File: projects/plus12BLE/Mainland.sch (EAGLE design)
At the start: 69 parts, among them J1 USB-CWM2.0, SW1 RSTSWSMD, SW2 RSTSWSMD, U1 BL652-SA-01-T/R, U2 MCP73831T-2ACI/OT, U4 CP2102N-A01-GQFN20

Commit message: working for DFM, new USB connector test
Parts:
- removed JP2: (no value), pinhead:PINHD-1X4
- removed JP3: (no value), pinhead:PINHD-1X5/90
- added J2: RA 6Pin SMD, SparkFun-Connectors:CONN_04SMD_RA_FEMALE
- added J3: RA 6Pin SMD, SparkFun-Connectors:CONN_06SMD
- C4, C6: device resistor:C-USC0402K -> resistor:C-USC0603
- R1, R10, R2, R3, R4, R5, R6, R7, R8, R9: device resistor:R-US_R0402 -> resistor:R-US_R0603
- SW1, SW2: value RSTSWSMD -> RSTSWSMALL_SMD; device Keys:RSTSWSMD -> Keys:RSTSWSMALL_SMD
- renumbered U$3 to SW3
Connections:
- net 3.3V: now also J2.4; no longer JP2.1, JP3.1
- net GND: now also J2.1, J3.1; no longer JP2.4, JP3.5
- net RX0: now also J3.5; no longer JP3.2
- net SWDCLK: now also J2.2; no longer JP2.3
- net SWDIO: now also J2.3; no longer JP2.2
- net TX0: now also J3.4; no longer JP3.3
- net V_USB: now also J3.3; no longer JP3.4
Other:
- note added: "Can also charge through V_USB and GND on this header"
- note added: "UART (RX/TX) Used in place of CP2104 QFN. MUST USE 3.3V LOGIC"
- note removed: "Also breaking out +5V Vbus/V_USB if soldering USBC is a difficulty"
- note removed: "UART (RX/TX) Used in place of CP2104 QFN"

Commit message: saving before autorouter
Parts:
- J1: value USB-CWM2.0 -> USB-C2.0WM2.0; device Keys:USB-CWM2.0 -> Keys:USB-C2.0WM2.0
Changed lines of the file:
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@@
 <grid distance="0.1" unitdist="inch" unit="inch" style="lines" multiple="1" display="no" altdistance="0.01" altunitdist="inch" altunit="inch"/>
 <layers>
-<layer number="1" name="Top" color="4" fill="1" visible="yes" active="no"/>
-<layer number="2" name="Route2" color="16" fill="1" visible="yes" active="no"/>
-<layer number="3" name="Route3" color="17" fill="1" visible="yes" active="no"/>
-<layer number="4" name="Route4" color="18" fill="1" visible="yes" active="no"/>
-<layer number="5" name="Route5" color="19" fill="1" visible="yes" active="no"/>
-<layer number="6" name="Route6" color="25" fill="1" visible="yes" active="no"/>
-<layer number="7" name="Route7" color="26" fill="1" visible="yes" active="no"/>
-<layer number="8" name="Route8" color="27" fill="1" visible="yes" active="no"/>
-<layer number="9" name="Route9" color="28" fill="1" visible="yes" active="no"/>
-<layer number="10" name="Route10" color="29" fill="1" visible="yes" active="no"/>
-<layer number="11" name="Route11" color="30" fill="1" visible="yes" active="no"/>
-<layer number="12" name="Route12" color="20" fill="1" visible="yes" active="no"/>
-<layer number="13" name="Route13" color="21" fill="1" visible="yes" active="no"/>
-<layer number="14" name="Route14" color="22" fill="1" visible="yes" active="no"/>
-<layer number="15" name="Route15" color="23" fill="1" visible="yes" active="no"/>
-<layer number="16" name="Bottom" color="1" fill="1" visible="yes" active="no"/>
-<layer number="17" name="Pads" color="2" fill="1" visible="yes" active="no"/>
-<layer number="18" name="Vias" color="2" fill="1" visible="yes" active="no"/>
-<layer number="19" name="Unrouted" color="6" fill="1" visible="yes" active="no"/>
-<layer number="20" name="Dimension" color="24" fill="1" visible="yes" active="no"/>
-<layer number="21" name="tPlace" color="7" fill="1" visible="yes" active="no"/>
-<layer number="22" name="bPlace" color="7" fill="1" visible="yes" active="no"/>
-<layer number="23" name="tOrigins" color="15" fill="1" visible="yes" active="no"/>
-<layer number="24" name="bOrigins" color="15" fill="1" visible="yes" active="no"/>
-<layer number="25" name="tNames" color="7" fill="1" visible="yes" active="no"/>
-<layer number="26" name="bNames" color="7" fill="1" visible="yes" active="no"/>
-<layer number="27" name="tValues" color="7" fill="1" visible="yes" active="no"/>
-<layer number="28" name="bValues" color="7" fill="1" visible="yes" active="no"/>
+<layer number="1" name="Top" color="4" fill="1" visible="no" active="no"/>
+<layer number="2" name="Route2" color="16" fill="1" visible="no" active="no"/>
+<layer number="3" name="Route3" color="17" fill="1" visible="no" active="no"/>
+<layer number="4" name="Route4" color="18" fill="1" visible="no" active="no"/>
+<layer number="5" name="Route5" color="19" fill="1" visible="no" active="no"/>
+<layer number="6" name="Route6" color="25" fill="1" visible="no" active="no"/>
+<layer number="7" name="Route7" color="26" fill="1" visible="no" active="no"/>
+<layer number="8" name="Route8" color="27" fill="1" visible="no" active="no"/>
+<layer number="9" name="Route9" color="28" fill="1" visible="no" active="no"/>
+<layer number="10" name="Route10" color="29" fill="1" visible="no" active="no"/>
+<layer number="11" name="Route11" color="30" fill="1" visible="no" active="no"/>
+<layer number="12" name="Route12" color="20" fill="1" visible="no" active="no"/>
+<layer number="13" name="Route13" color="21" fill="1" visible="no" active="no"/>
+<layer number="14" name="Route14" color="22" fill="1" visible="no" active="no"/>
+<layer number="15" name="Route15" color="23" fill="1" visible="no" active="no"/>
+<layer number="16" name="Bottom" color="1" fill="1" visible="no" active="no"/>
+<layer number="17" name="Pads" color="2" fill="1" visible="no" active="no"/>
+<layer number="18" name="Vias" color="2" fill="1" visible="no" active="no"/>
+<layer number="19" name="Unrouted" color="6" fill="1" visible="no" active="no"/>
+<layer number="20" name="Dimension" color="24" fill="1" visible="no" active="no"/>
+<layer number="21" name="tPlace" color="7" fill="1" visible="no" active="no"/>
+<layer number="22" name="bPlace" color="7" fill="1" visible="no" active="no"/>
+<layer number="23" name="tOrigins" color="15" fill="1" visible="no" active="no"/>
+<layer number="24" name="bOrigins" color="15" fill="1" visible="no" active="no"/>
+<layer number="25" name="tNames" color="7" fill="1" visible="no" active="no"/>
+<layer number="26" name="bNames" color="7" fill="1" visible="no" active="no"/>
+<layer number="27" name="tValues" color="7" fill="1" visible="no" active="no"/>
+<layer number="28" name="bValues" color="7" fill="1" visible="no" active="no"/>
 <layer number="29" name="tStop" color="7" fill="3" visible="no" active="no"/>
 <layer number="30" name="bStop" color="7" fill="6" visible="no" active="no"/>
@@
 <layer number="35" name="tGlue" color="7" fill="4" visible="no" active="no"/>
 <layer number="36" name="bGlue" color="7" fill="5" visible="no" active="no"/>
-<layer number="37" name="tTest" color="7" fill="1" visible="yes" active="no"/>
-<layer number="38" name="bTest" color="7" fill="1" visible="yes" active="no"/>
+<layer number="37" name="tTest" color="7" fill="1" visible="no" active="no"/>
+<layer number="38" name="bTest" color="7" fill="1" visible="no" active="no"/>
 <layer number="39" name="tKeepout" color="4" fill="11" visible="no" active="no"/>
 <layer number="40" name="bKeepout" color="1" fill="11" visible="no" active="no"/>
@@
 <layer number="44" name="Drills" color="7" fill="1" visible="no" active="no"/>
 <layer number="45" name="Holes" color="7" fill="1" visible="no" active="no"/>
-<layer number="46" name="Milling" color="3" fill="1" visible="yes" active="no"/>
-<layer number="47" name="Measures" color="7" fill="1" visible="yes" active="no"/>
-<layer number="48" name="Document" color="7" fill="1" visible="yes" active="no"/>
-<layer number="49" name="Reference" color="7" fill="1" visible="yes" active="no"/>
-<layer number="50" name="dxf" color="7" fill="1" visible="yes" active="no"/>
-<layer number="51" name="tDocu" color="7" fill="1" visible="yes" active="no"/>
-<layer number="52" name="bDocu" color="7" fill="1" visible="yes" active="no"/>
-<layer number="53" name="tGND_GNDA" color="7" fill="9" visible="yes" active="no"/>
-<layer number="54" name="bGND_GNDA" color="1" fill="9" visible="yes" active="no"/>
-<layer number="56" name="wert" color="7" fill="1" visible="yes" active="no"/>
-<layer number="57" name="tCAD" color="7" fill="1" visible="yes" active="no"/>
-<layer number="59" name="tCarbon" color="7" fill="1" visible="yes" active="no"/>
-<layer number="60" name="bCarbon" color="7" fill="1" visible="yes" active="no"/>
+<layer number="46" name="Milling" color="3" fill="1" visible="no" active="no"/>
+<layer number="47" name="Measures" color="7" fill="1" visible="no" active="no"/>
+<layer number="48" name="Document" color="7" fill="1" visible="no" active="no"/>
+<layer number="49" name="Reference" color="7" fill="1" visible="no" active="no"/>
+<layer number="50" name="dxf" color="7" fill="1" visible="no" active="no"/>
+<layer number="51" name="tDocu" color="7" fill="1" visible="no" active="no"/>
+<layer number="52" name="bDocu" color="7" fill="1" visible="no" active="no"/>
+<layer number="53" name="tGND_GNDA" color="7" fill="9" visible="no" active="no"/>
+<layer number="54" name="bGND_GNDA" color="1" fill="9" visible="no" active="no"/>
+<layer number="56" name="wert" color="7" fill="1" visible="no" active="no"/>
+<layer number="57" name="tCAD" color="7" fill="1" visible="no" active="no"/>
+<layer number="59" name="tCarbon" color="7" fill="1" visible="no" active="no"/>
+<layer number="60" name="bCarbon" color="7" fill="1" visible="no" active="no"/>
 <layer number="88" name="SimResults" color="9" fill="1" visible="yes" active="yes"/>
 <layer number="89" name="SimProbes" color="9" fill="1" visible="yes" active="yes"/>
@@
 <part name="GND7" library="SparkFun-PowerSymbols" library_urn="urn:adsk.eagle:library:530" deviceset="GND" device=""/>
 <part name="GND8" library="SparkFun-PowerSymbols" library_urn="urn:adsk.eagle:library:530" deviceset="GND" device=""/>
-<part name="J1" library="Keys" deviceset="USB-C" device="WM2.0" value="USB-CWM2.0"/>
+<part name="J1" library="Keys" deviceset="USB-C2.0" device="WM2.0" value="USB-C2.0WM2.0"/>
 <part name="R1" library="resistor" library_urn="urn:adsk.eagle:library:348" deviceset="R-US_" device="R0603" package3d_urn="urn:adsk.eagle:package:23555/2" value="5.1k"/>
 <part name="JP1" library="pinhead" library_urn="urn:adsk.eagle:library:325" deviceset="PINHD-1X2" device="" package3d_urn="urn:adsk.eagle:package:22435/2"/>

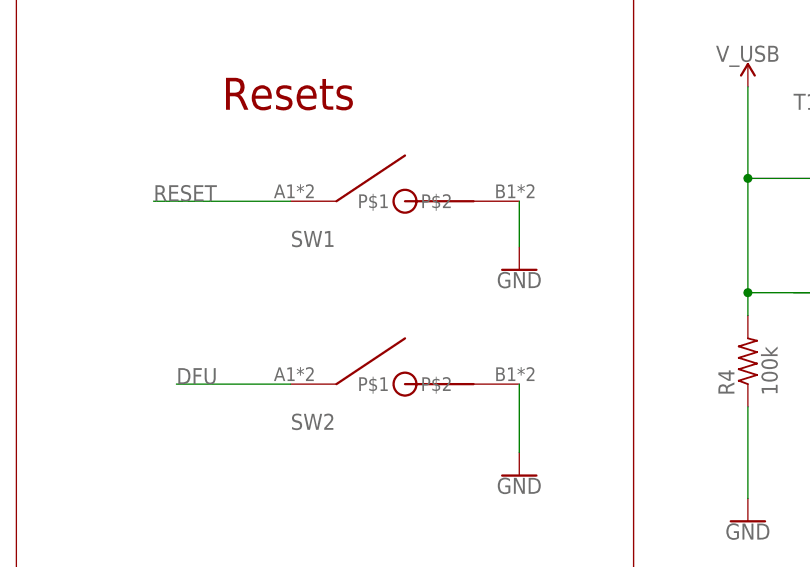
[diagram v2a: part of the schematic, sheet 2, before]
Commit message: revB of plus12BLE and necessary library changes
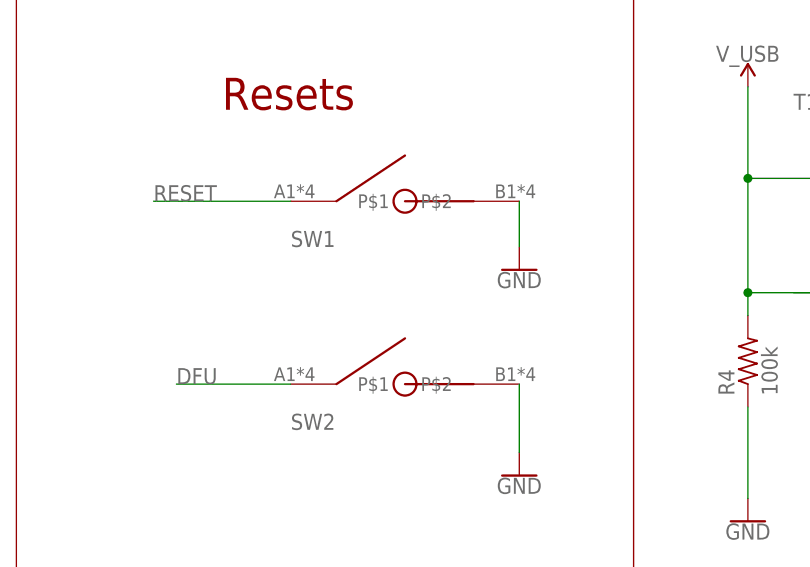
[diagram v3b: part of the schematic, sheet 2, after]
